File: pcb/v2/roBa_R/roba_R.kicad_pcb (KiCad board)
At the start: 2 copper layers, 123.9 x 94.5 mm, 50 parts, among them J2 Conn_01x01-Connector_Generic, J3 Conn_01x01-Connector_Generic, J4 Conn_01x01-Connector_Generic, J5 Conn_01x01-Connector_Generic, J6 Conn_01x01-Connector_Generic, J7 Conn_01x01-Connector_Generic, SW1 SW_PUSH, SW10 SW_PUSH, SW11 SW_PUSH, SW12 SW_PUSH, SW13 SW_PUSH, SW14 SW_PUSH, SW15 SW_PUSH, SW16 SW_PUSH, SW17 SW_PUSH, SW18 SW_PUSH, SW19 SW_PUSH, SW2 SW_PUSH, SW20 SW_PUSH, SW21 SW_SPDT, SW3 SW_PUSH, SW4 SW_PUSH, SW5 SW_PUSH, SW6 SW_PUSH, SW7 SW_PUSH, SW8 SW_PUSH, SW9 SW_PUSH

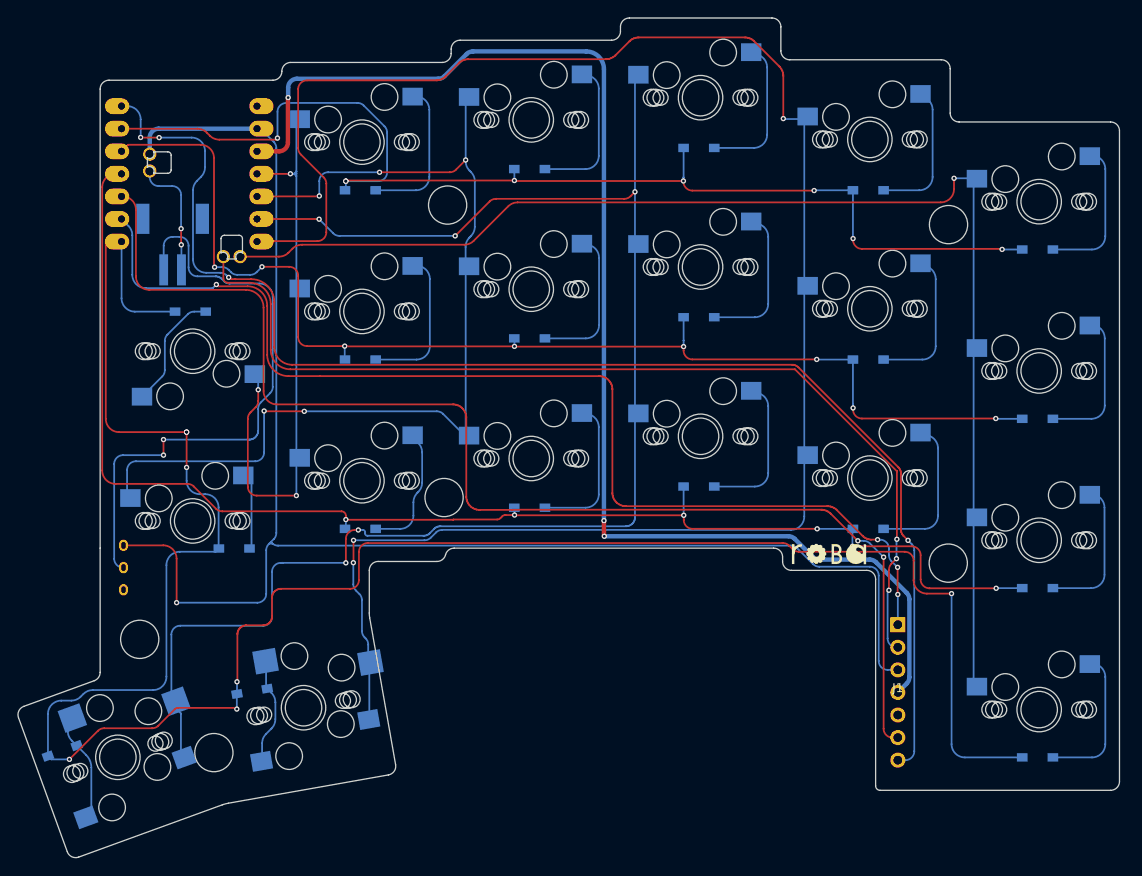
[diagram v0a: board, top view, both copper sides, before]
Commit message: Add VIK connector to trackball PCB, Remove earlier revisions
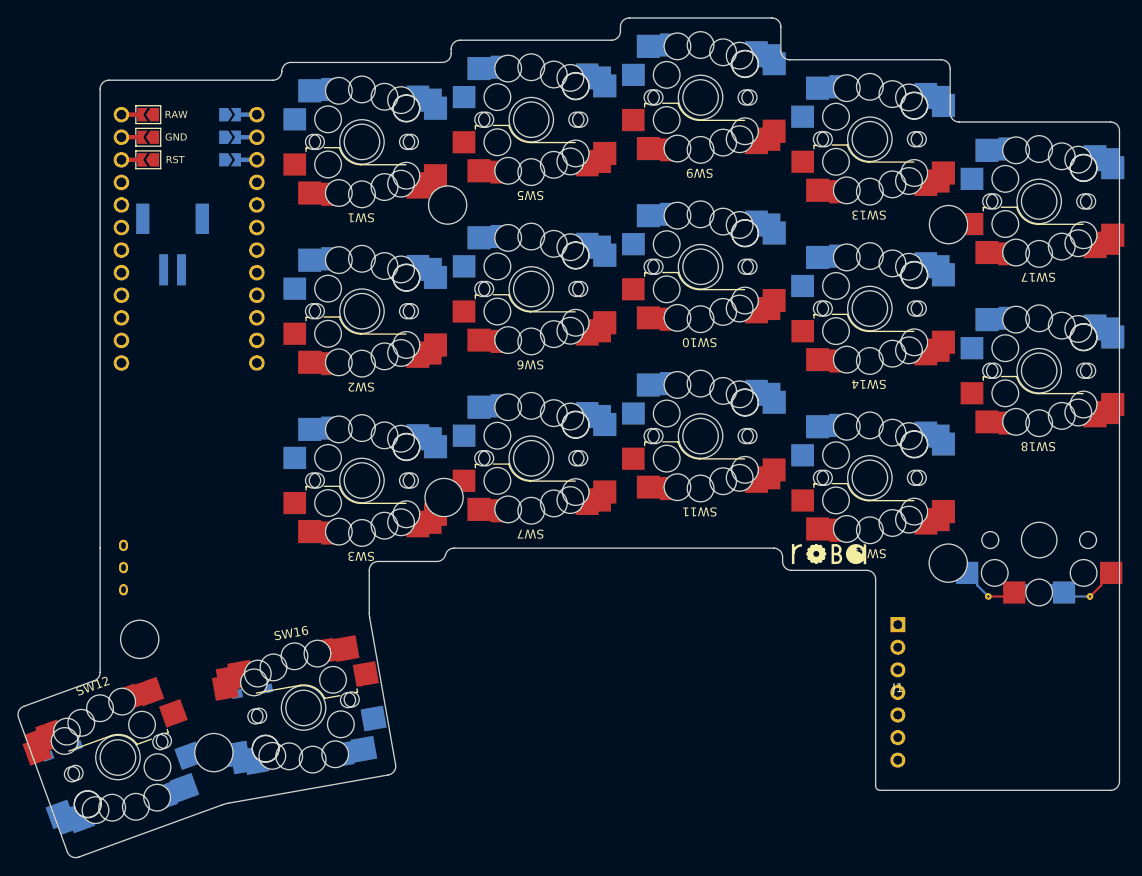
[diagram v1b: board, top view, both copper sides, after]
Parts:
- removed D20, D4, D8: D, roBa:Diode_SMD
- removed SW20, SW4, SW8: SW_PUSH, roBa:SW_MX
- SW1, SW10, SW11, SW13, SW14, SW15, SW17, SW18, SW2, SW3, SW5, SW6, SW7, SW9: footprint roBa:SW_MX -> fingerpunch:gateron-ks27-choc-v1-mx-hotswap-reversible
- SW12, SW16: footprint roBa:SW_MX_Choc -> fingerpunch:gateron-ks27-choc-v1-mx-hotswap-reversible
- SW19: footprint roBa:SW_MX -> keyboard_reversible:Choc_Hotswap
- U1: footprint roBa:XIAO_nRF52840_wBAT_wNFC_1 -> footprints:ProMicroSimpleJumper
- moved U1 17.8 mm to (109.9, 80.3), turned to -90 degrees
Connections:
- U1 pad 1: MOTION -> unconnected-(U1-TX0/D3-Pad1)
- U1 pad 10: Col1 -> unconnected-(U1-7/E6-Pad10)
- U1 pad 11: Col0 -> unconnected-(U1-8/B4-Pad11)
- U1 pad 12: 3.3V -> unconnected-(U1-9/B5-Pad12)
- U1 pad 2: Row0 -> unconnected-(U1-RX1/D2-Pad2)
- U1 pad 20: Bat -> unconnected-(U1-F4/A3-Pad20)
- U1 pad 21: GND -> unconnected-(U1-VCC-Pad21)
- U1 pad 3: Row1 -> unconnected-(U1-GND-Pad3)
- U1 pad 5: SDIO -> unconnected-(U1-2/D1/SDA-Pad5)
- U1 pad 6: SCLK -> unconnected-(U1-3/D0/SCL-Pad6)
- U1 pad 7: Row3 -> unconnected-(U1-4/D4-Pad7)
- U1 pad 8: Col3 -> unconnected-(U1-5/C6-Pad8)
- U1 pad 9: Col2 -> unconnected-(U1-6/D7-Pad9)
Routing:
- net Row3: track 249.7 -> 0.00 mm, vias 7 -> 0
- net Col3: track 209.2 -> 0.00 mm, vias 3 -> 0
- net GND: track 173.8 -> 0.00 mm, vias 1 -> 0
- net Col2: track 172.6 -> 0.00 mm, vias 5 -> 0
- net Row2: track 153.3 -> 0.00 mm, vias 6 -> 0
- net MOTION: track 153.2 -> 0.00 mm, vias 4 -> 0
- net 3.3V: track 149.3 -> 0.00 mm, vias 3 -> 0
- net Col4: track 143.9 -> 0.00 mm, vias 1 -> 0
- net SDIO: track 140.2 -> 0.00 mm, vias 2 -> 0
- net Row1: track 136.2 -> 0.00 mm, vias 8 -> 0
- net Row0: track 134.2 -> 0.00 mm, vias 8 -> 0
- net SCLK: track 125.1 -> 0.00 mm, vias 4 -> 0
- net Col1: track 113.2 -> 0.00 mm, vias 5 -> 0
- net CS: track 111.9 -> 0.00 mm, vias 3 -> 0
- net Net-(BT1--): track 67.0 -> 0.00 mm, vias 2 -> 0
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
